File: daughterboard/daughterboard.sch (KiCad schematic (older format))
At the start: 34 parts, among them CON1 12V_JACK, IC1 ATMEGA328P-A, P1 EXTRA_PB01, P2 EXTRA_PC12345, P3 CONN_13X2, P4 AZIMUTH, P5 ELEVATION, P6 EXTRA_ADC67, P7 VALVE, Q1 TIP120, U1 ULN2803A, Y1 8MHz

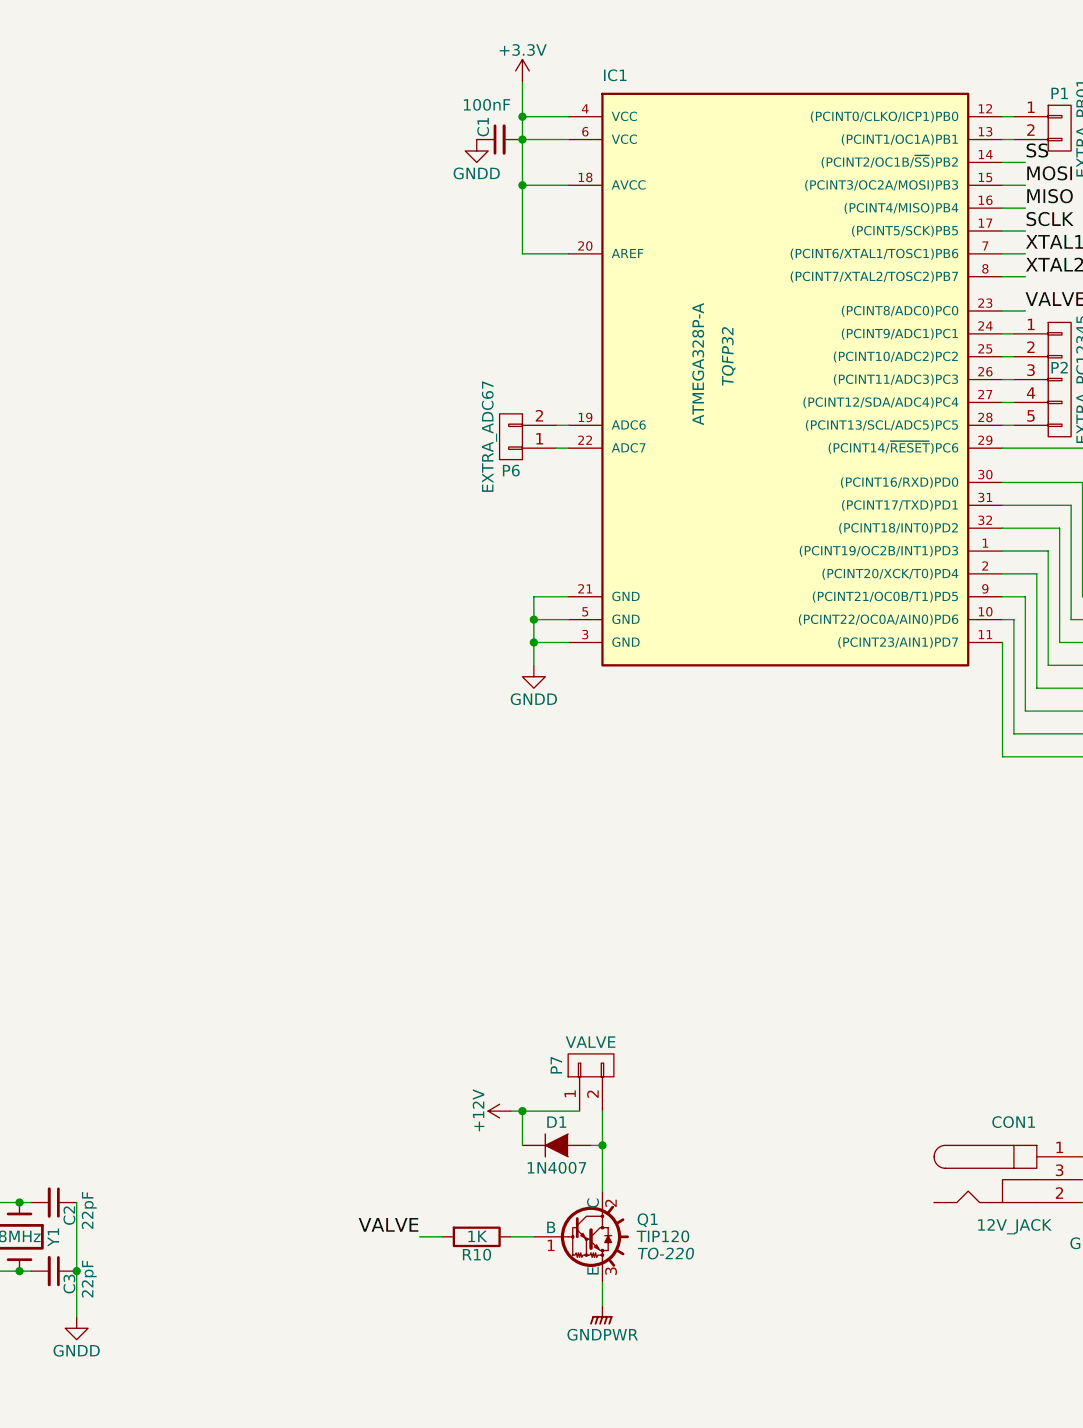
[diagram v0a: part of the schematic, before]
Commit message: Generate netlist, choose footprints
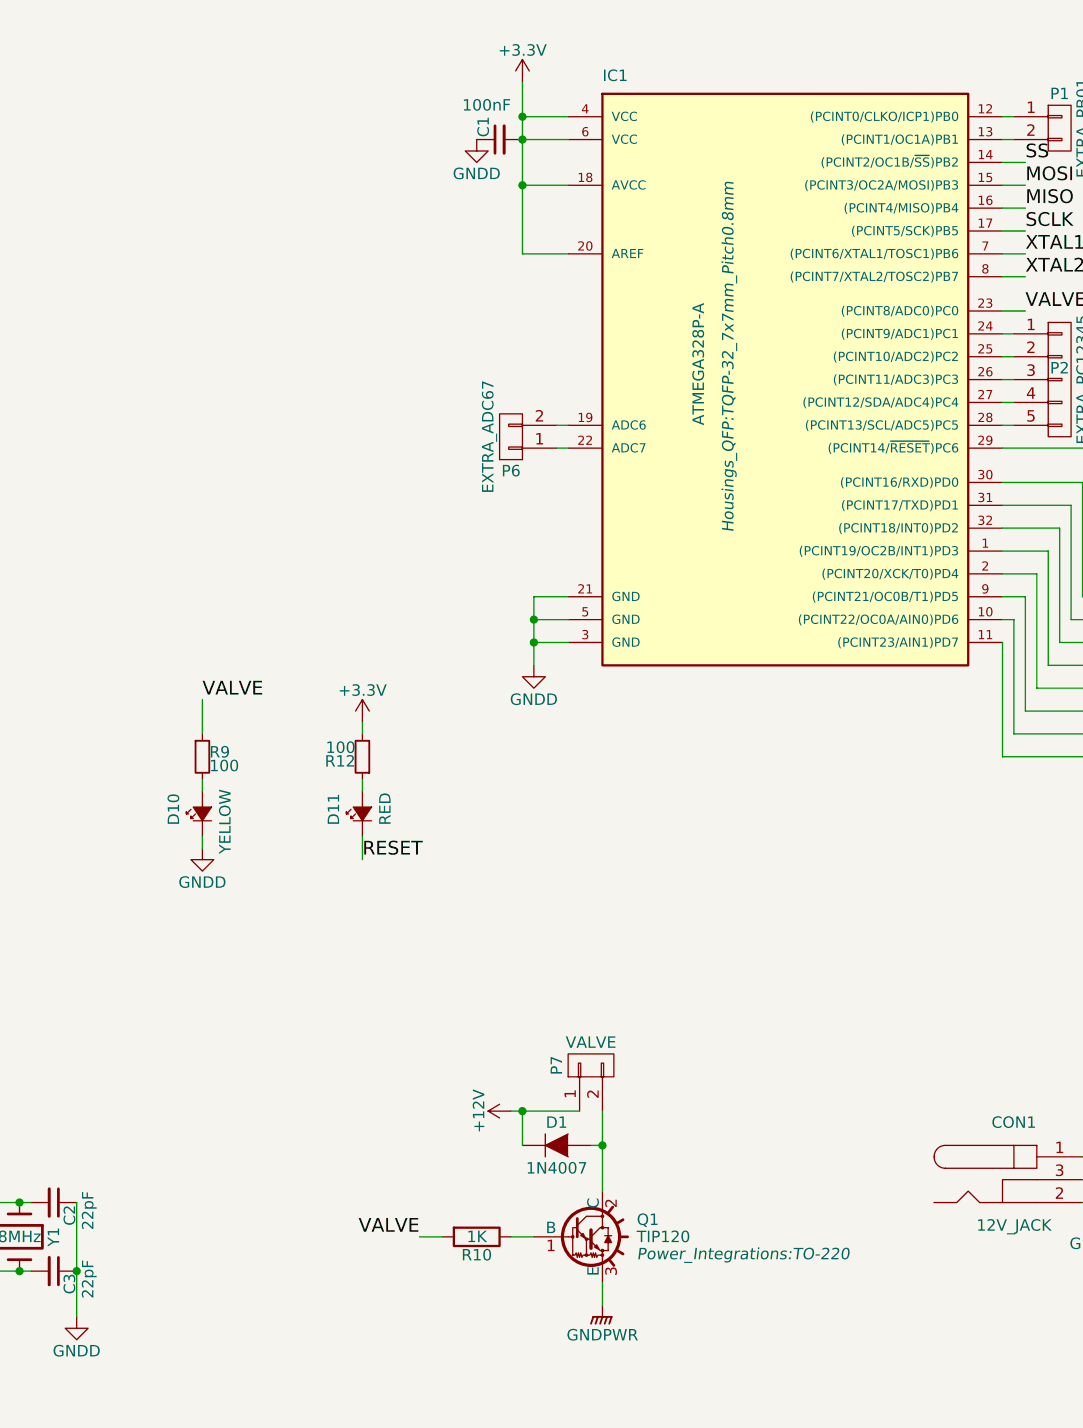
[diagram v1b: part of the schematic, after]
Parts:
- added D10: YELLOW, LEDs:LED_0805, symbol Led_Small
- added D11: RED, LEDs:LED_0805, symbol Led_Small
- added R12, R9: 100, Resistors_SMD:R_0805_HandSoldering, symbol R_Small
- C1, C2, C3: footprint (none) -> Capacitors_SMD:C_0805_HandSoldering
- CON1: footprint (none) -> Connect:BARREL_JACK
- D1: footprint (none) -> Diodes_ThroughHole:Diode_DO-41_SOD81_Vertical_AnodeUp
- D2, D3, D4, D5, D6, D7, D8, D9: footprint (none) -> LEDs:LED_0805
- IC1: footprint TQFP32 -> Housings_QFP:TQFP-32_7x7mm_Pitch0.8mm
- P1, P6, P7: footprint (none) -> Pin_Headers:Pin_Header_Straight_1x02
- P2: footprint (none) -> Pin_Headers:Pin_Header_Straight_1x05
- P3: footprint (none) -> Pin_Headers:Pin_Header_Straight_2x13
- P4, P5: footprint (none) -> Pin_Headers:Pin_Header_Straight_1x04
- Q1: footprint TO-220 -> Power_Integrations:TO-220
- R1, R10, R11, R2: footprint (none) -> Resistors_SMD:R_0805_HandSoldering
- R3, R4, R5, R6, R7, R8: value (none) -> 500; footprint (none) -> Resistors_SMD:R_0805_HandSoldering
- U1: footprint (none) -> Housings_SOIC:SOIC-18_7.5x11.6mm_Pitch1.27mm
- Y1: footprint (none) -> Crystals:HC-49V
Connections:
- net +3V3: now also R12.2
- net GNDD: now also D10.1 (K)
- net GPIO25: now also D11.1 (K)
- net VALVE: now also R9.1
- new net: D11.2 (A), R12.1
- new net: D10.2 (A), R9.2

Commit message: fix pin assignments
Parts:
- P4, P5: footprint Pin_Headers:Pin_Header_Straight_1x04 -> Pin_Headers:Pin_Header_Straight_1x05
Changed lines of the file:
@@
 F 0 "P4" H 10750 3150 50  0000 C CNN
 F 1 "AZIMUTH" V 10850 2850 50  0000 C CNN
-F 2 "Pin_Headers:Pin_Header_Straight_1x04" H 10750 2850 50  0001 C CNN
+F 2 "Pin_Headers:Pin_Header_Straight_1x05" H 10750 2850 50  0001 C CNN
 F 3 "" H 10750 2850 50  0000 C CNN
 	1    10750 2850
@@
 F 0 "P5" H 10750 4700 50  0000 C CNN
 F 1 "ELEVATION" V 10850 4400 50  0000 C CNN
-F 2 "Pin_Headers:Pin_Header_Straight_1x04" H 10750 4400 50  0001 C CNN
+F 2 "Pin_Headers:Pin_Header_Straight_1x05" H 10750 4400 50  0001 C CNN
 F 3 "" H 10750 4400 50  0000 C CNN
 	1    10750 4400

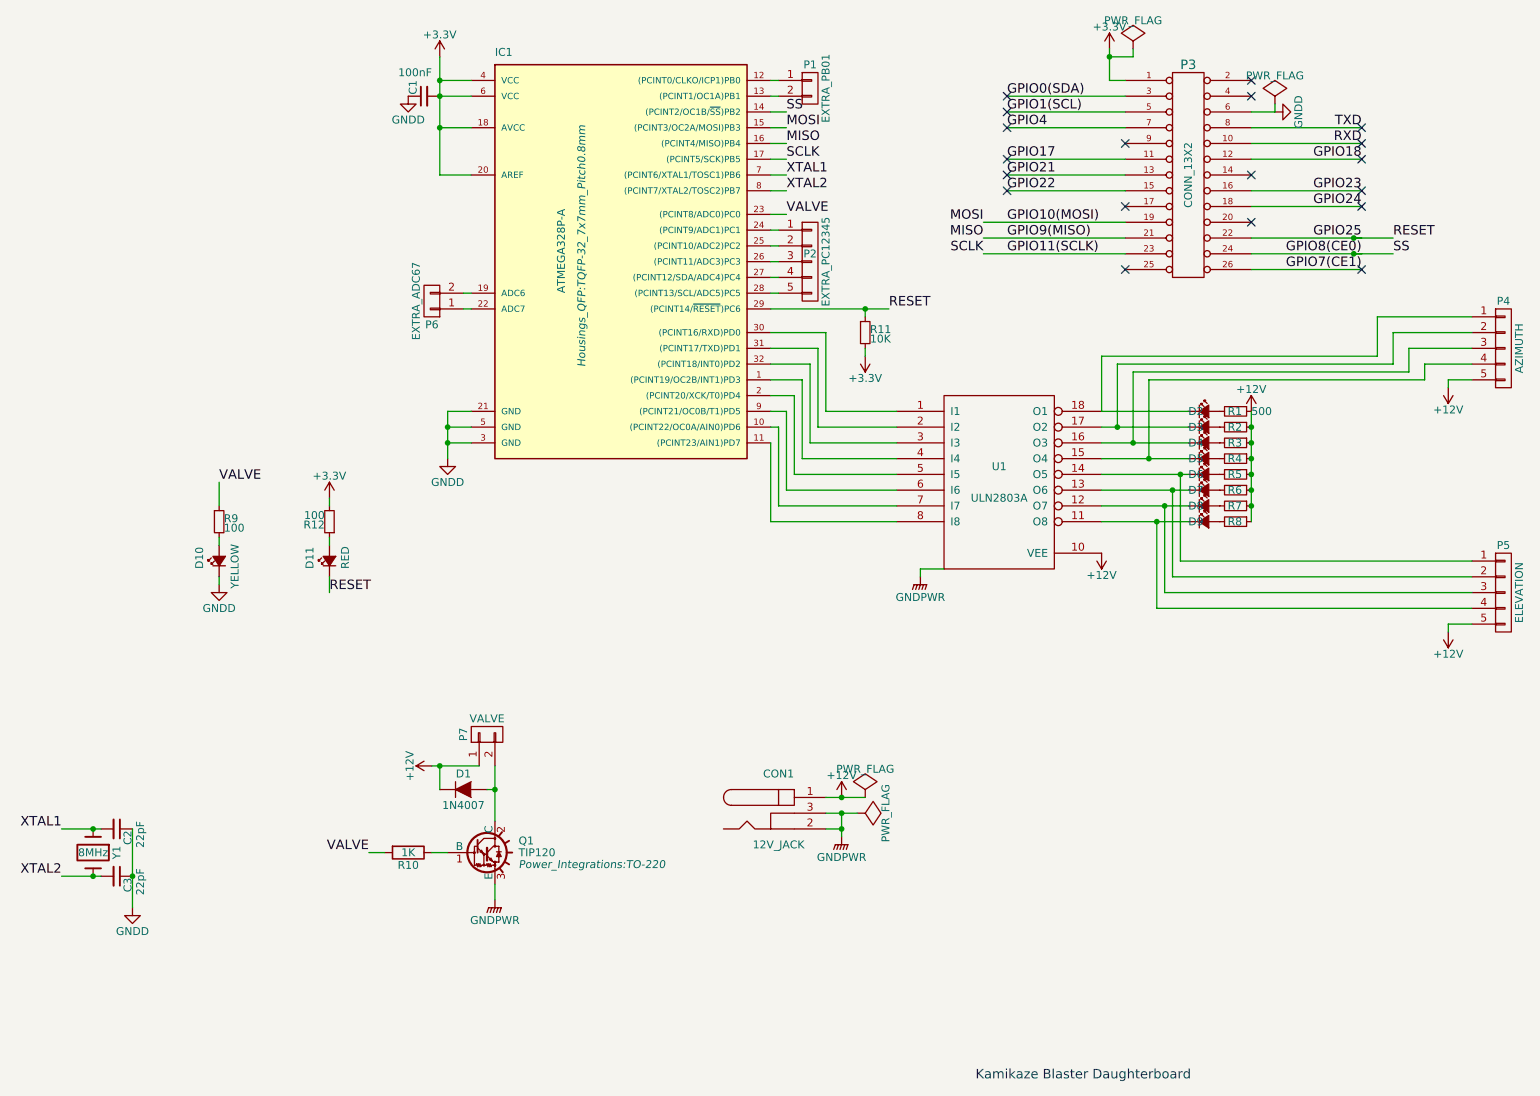
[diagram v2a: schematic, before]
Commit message: Reassign pins around to simplify layout
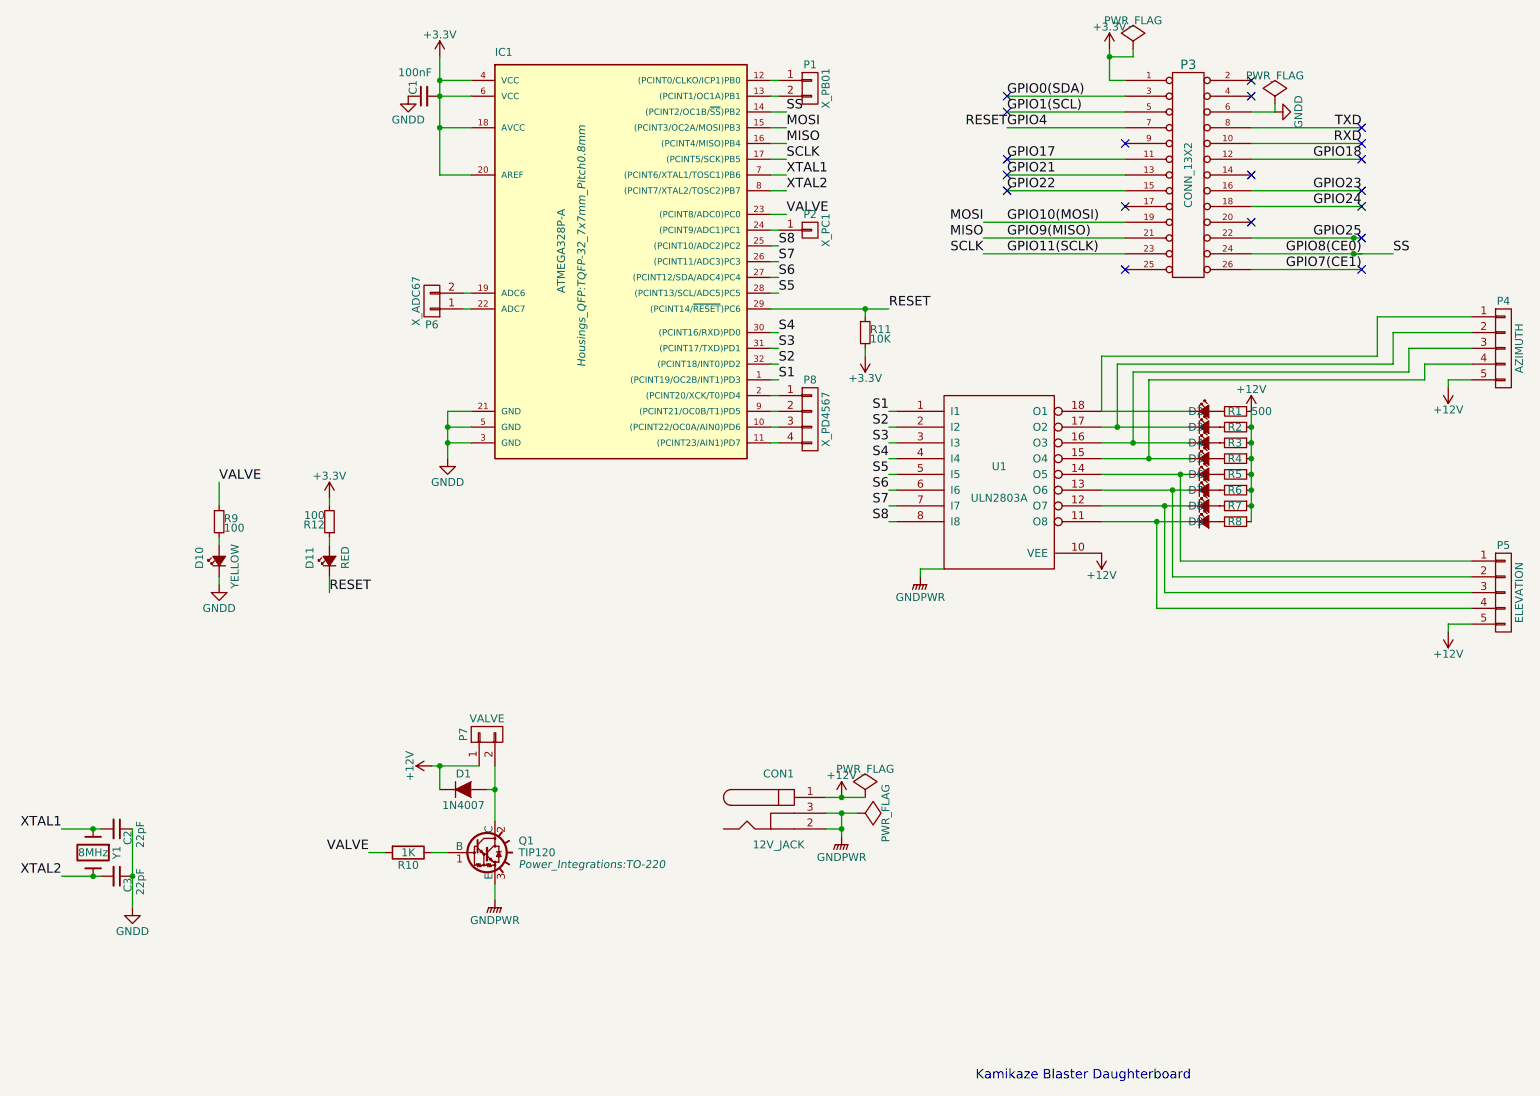
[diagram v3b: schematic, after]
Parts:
- removed P2: EXTRA_PC12345, Pin_Headers:Pin_Header_Straight_1x05, symbol CONN_01X05
- added P2: X_PC1, symbol CONN_01X01
- added P8: X_PD4567, symbol CONN_01X04
- P1: value EXTRA_PB01 -> X_PB01
- P6: value EXTRA_ADC67 -> X_ADC67
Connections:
- net GPIO25: no longer D11.1 (K), IC1.29 ((PCINT14/~RESET~)PC6), R11.1
- net GPIO4: now also D11.1 (K), IC1.29 ((PCINT14/~RESET~)PC6), R11.1
- net S1: now reaches IC1.1 ((PCINT19/OC2B/INT1)PD3)
- net S1: now also U1.1 (I1); no longer U1.4 (I4)
- net at IC1.10 ((PCINT22/OC0A/AIN0)PD6): now also P8.3 (P3); no longer U1.7 (I7)
- net at IC1.11 ((PCINT23/AIN1)PD7): now also P8.4 (P4); no longer U1.8 (I8)
- net at IC1.2 ((PCINT20/XCK/T0)PD4): now also P8.1 (P1); no longer U1.5 (I5)
- net at IC1.24 ((PCINT9/ADC1)PC1): now also P2.1 (P1)
- net S8: now reaches IC1.25 ((PCINT10/ADC2)PC2)
- net S8: now also U1.8 (I8)
- net S7: now reaches IC1.26 ((PCINT11/ADC3)PC3)
- net S7: now also U1.7 (I7)
- net S6: now reaches IC1.27 ((PCINT12/SDA/ADC4)PC4)
- net S6: now also U1.6 (I6)
- net S5: now reaches IC1.28 ((PCINT13/SCL/ADC5)PC5)
- net S5: now also U1.5 (I5)
- net S4: now reaches IC1.30 ((PCINT16/RXD)PD0)
- net S4: now also U1.4 (I4); no longer U1.1 (I1)
- net S2: now reaches U1.2 (I2)
- net S2: now also IC1.32 ((PCINT18/INT0)PD2); no longer IC1.31 ((PCINT17/TXD)PD1)
- net S3: now reaches U1.3 (I3)
- net S3: now also IC1.31 ((PCINT17/TXD)PD1); no longer IC1.32 ((PCINT18/INT0)PD2)
- net at IC1.9 ((PCINT21/OC0B/T1)PD5): now also P8.2 (P2); no longer U1.6 (I6)

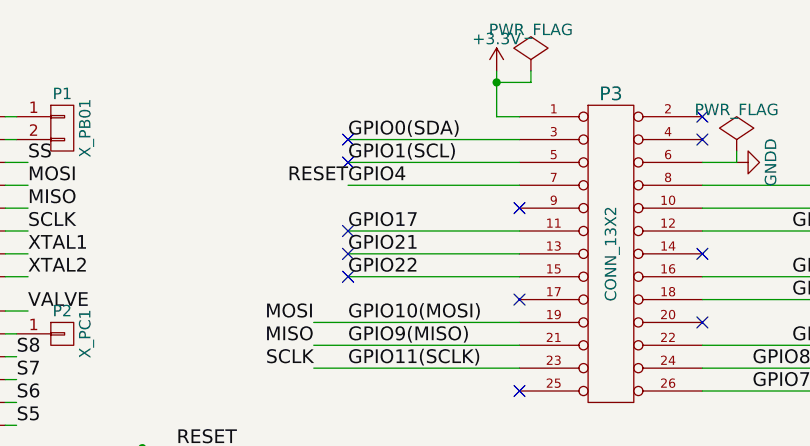
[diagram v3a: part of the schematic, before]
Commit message: Route everything except optional headers
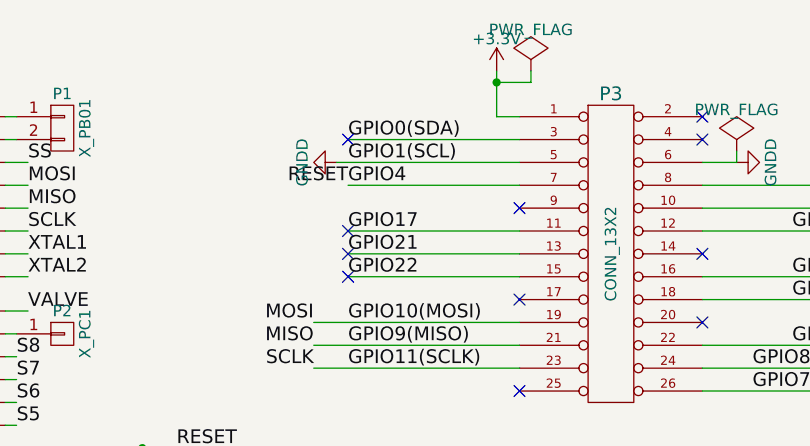
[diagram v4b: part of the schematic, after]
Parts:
- P2: footprint (none) -> Pin_Headers:Pin_Header_Straight_1x01
- P8: footprint (none) -> Pin_Headers:Pin_Header_Straight_1x04
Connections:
- net GPIO1(SCL) is gone; now on net GNDD: P3.5 (P5)
- no-connect marks 19 -> 18
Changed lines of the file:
@@
 $EndComp
 NoConn ~ 7600 1250
-NoConn ~ 7600 1350
 NoConn ~ 7600 1650
 NoConn ~ 7600 1750
@@
 	8350 1450 7600 1450
 Wire Wire Line
-	8350 1350 7600 1350
+	7550 1350 8350 1350
 Wire Wire Line
 	8350 1250 7600 1250
@@
 F 0 "P8" H 6350 3550 50  0000 C CNN
 F 1 "X_PD4567" V 6450 3300 50  0000 C CNN
-F 2 "" H 6350 3300 50  0000 C CNN
+F 2 "Pin_Headers:Pin_Header_Straight_1x04" H 6350 3300 50  0001 C CNN
 F 3 "" H 6350 3300 50  0000 C CNN
 	1    6350 3300
@@
 F 0 "P2" H 6350 2200 50  0000 C CNN
 F 1 "X_PC1" V 6450 2100 50  0000 C CNN
-F 2 "" H 6350 2100 50  0000 C CNN
+F 2 "Pin_Headers:Pin_Header_Straight_1x01" H 6350 2100 50  0001 C CNN
 F 3 "" H 6350 2100 50  0000 C CNN
 	1    6350 2100
@@
 Wire Wire Line
 	6100 2100 6150 2100
+$Comp
+L GNDD #PWR023
+U 1 1 5A084405
+P 7550 1350
+F 0 "#PWR023" H 7550 1100 50  0001 C CNN
+F 1 "GNDD" H 7550 1200 50  0000 C CNN
+F 2 "" H 7550 1350 50  0000 C CNN
+F 3 "" H 7550 1350 50  0000 C CNN
+	1    7550 1350
+	0    1    1    0
+$EndComp
 $EndSCHEMATC

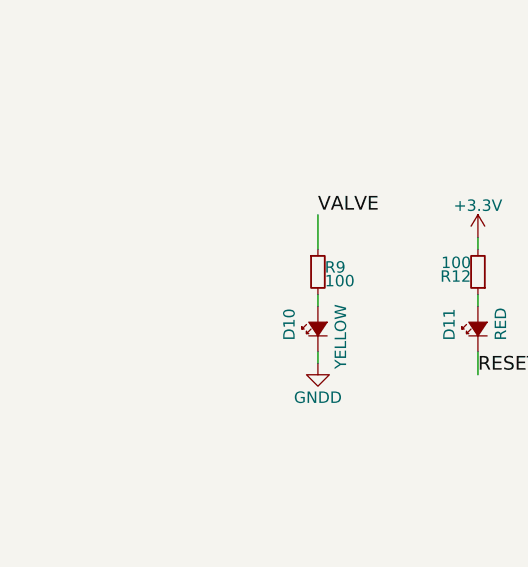
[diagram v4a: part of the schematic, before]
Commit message: Tweak footprint for barrel jack, move unused port off board / tweak trace
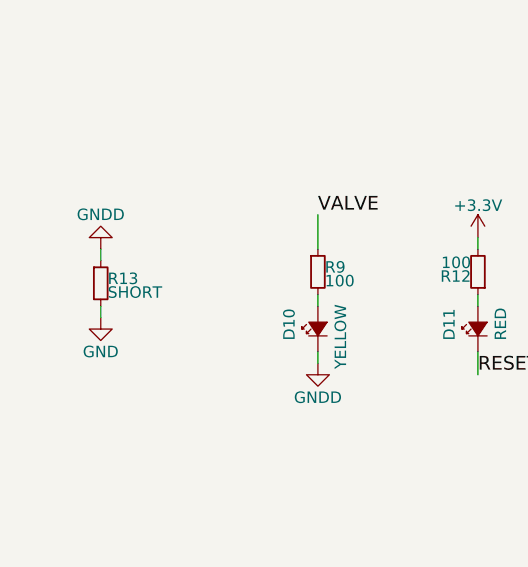
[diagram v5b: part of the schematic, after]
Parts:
- added R13: SHORT, Resistors_ThroughHole:Resistor_Vertical_RM5mm, symbol R_Small
- CON1: footprint Connect:BARREL_JACK -> footprints:BARREL_JACK
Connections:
- net GND: now also R13.2
- net GNDD: now also R13.1
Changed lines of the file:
@@
 F 0 "CON1" H 6150 6050 50  0000 C CNN
 F 1 "12V_JACK" H 6150 5600 50  0000 C CNN
-F 2 "Connect:BARREL_JACK" H 6150 5800 50  0001 C CNN
+F 2 "footprints:BARREL_JACK" H 6150 5800 50  0001 C CNN
 F 3 "" H 6150 5800 50  0000 C CNN
 	1    6150 5800
@@
 	0    1    1    0
 $EndComp
+$Comp
+L R_Small R13
+U 1 1 5A085791
+P 1650 4000
+F 0 "R13" H 1680 4020 50  0000 L CNN
+F 1 "SHORT" H 1680 3960 50  0000 L CNN
+F 2 "Resistors_ThroughHole:Resistor_Vertical_RM5mm" H 1650 4000 50  0001 C CNN
+F 3 "" H 1650 4000 50  0000 C CNN
+	1    1650 4000
+	1    0    0    -1
+$EndComp
+$Comp
+L GND #PWR024
+U 1 1 5A085806
+P 1650 4150
+F 0 "#PWR024" H 1650 3900 50  0001 C CNN
+F 1 "GND" H 1650 4000 50  0000 C CNN
+F 2 "" H 1650 4150 50  0000 C CNN
+F 3 "" H 1650 4150 50  0000 C CNN
+	1    1650 4150
+	1    0    0    -1
+$EndComp
+$Comp
+L GNDD #PWR025
+U 1 1 5A08586A
+P 1650 3850
+F 0 "#PWR025" H 1650 3600 50  0001 C CNN
+F 1 "GNDD" H 1650 3700 50  0000 C CNN
+F 2 "" H 1650 3850 50  0000 C CNN
+F 3 "" H 1650 3850 50  0000 C CNN
+	1    1650 3850
+	-1   0    0    1
+$EndComp
+Wire Wire Line
+	1650 3850 1650 3900
+Wire Wire Line
+	1650 4100 1650 4150
 $EndSCHEMATC
